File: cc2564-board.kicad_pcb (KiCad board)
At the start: 2 copper layers, 45 parts, among them J1 TYPE-C-31-M-12, J2 Conn_ARM_JTAG_SWD_10, J4 BOOT1, J5 BOOT0, J6 Conn_01x16, J7 Conn_01x16, U1 LD1117#33, U2 LD1117#18, U3 STM32F103C8Tx, U4 CC2564CRVMR, U5 TXB0104D

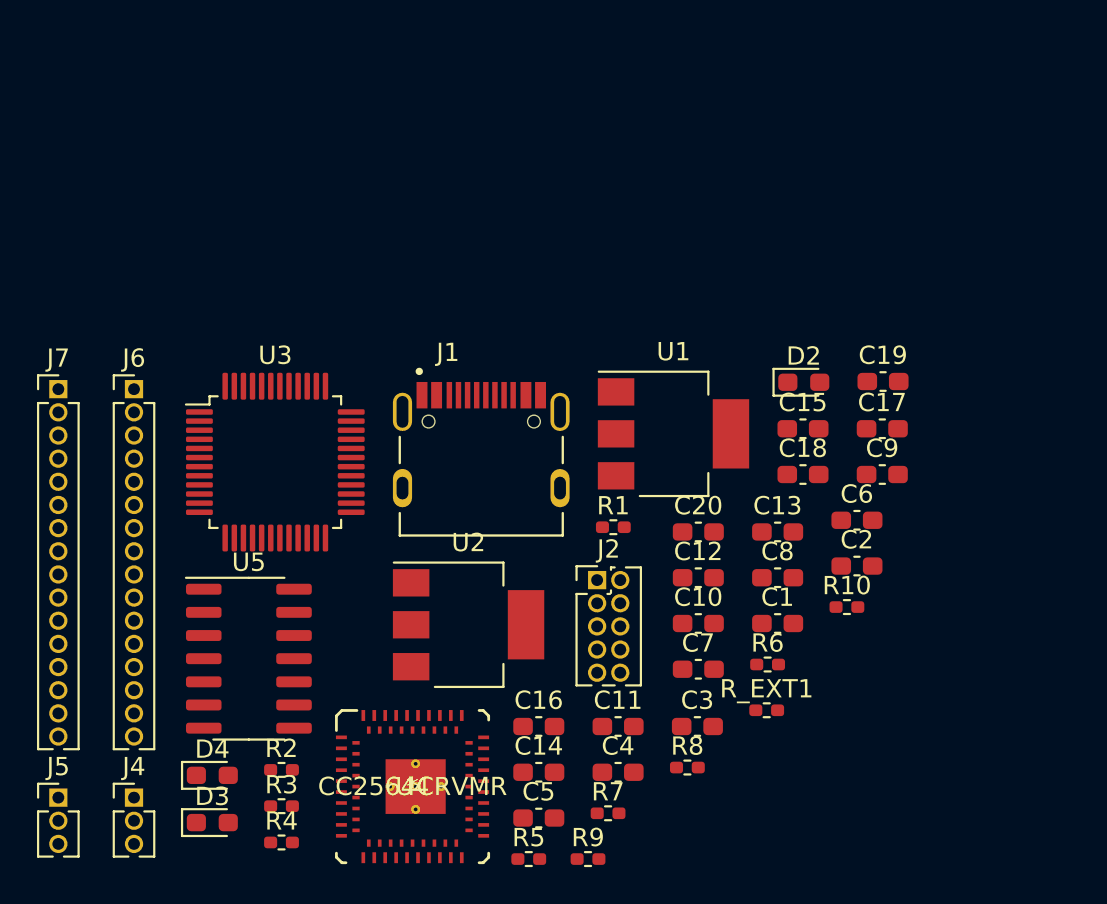
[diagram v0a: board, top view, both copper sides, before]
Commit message: RF matching placeholder and filtering
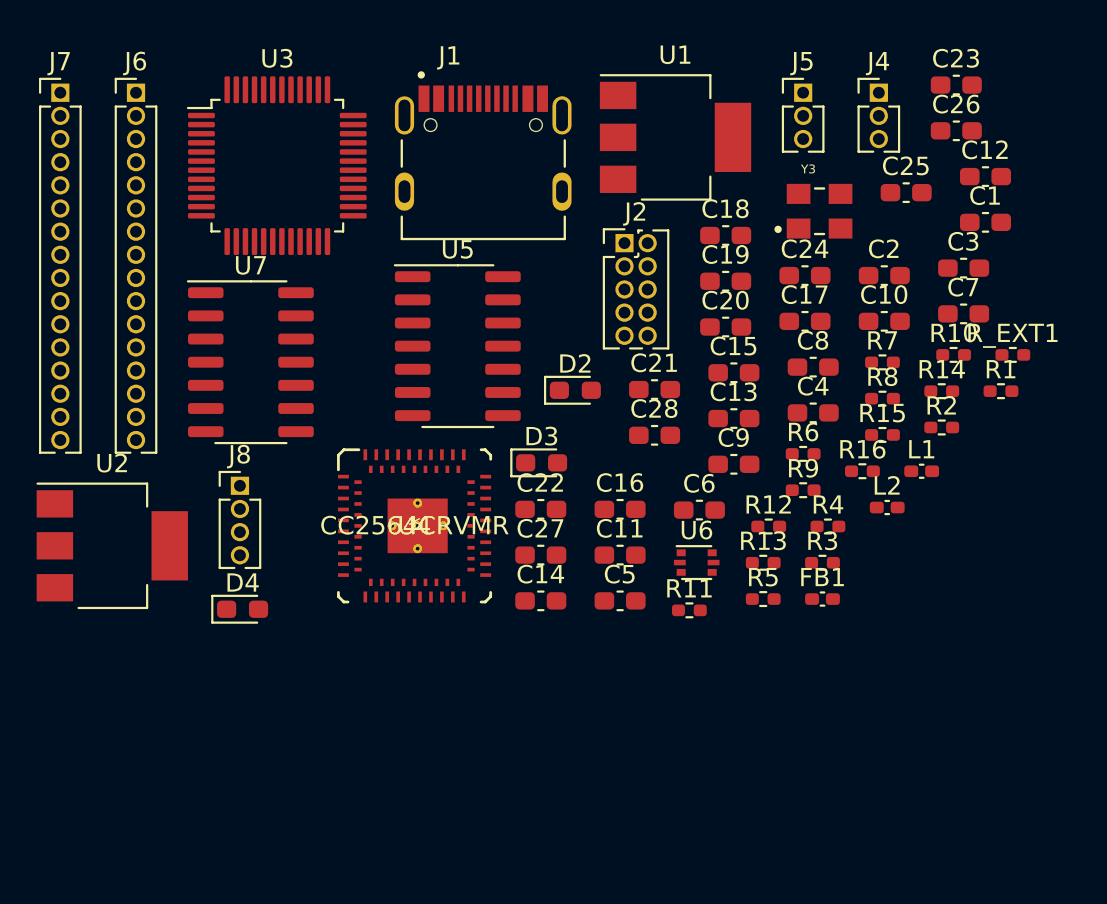
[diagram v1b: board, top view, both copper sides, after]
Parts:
- added C21: 10 pF, Capacitor_SMD:C_0603_1608Metric_Pad1.08x0.95mm_HandSolder, F.Cu at (131.4, 80.0)
- added C22: 10 pF, Capacitor_SMD:C_0603_1608Metric_Pad1.08x0.95mm_HandSolder, F.Cu at (125.2, 86.5)
- added C23: 0.1uF, Capacitor_SMD:C_0603_1608Metric_Pad1.08x0.95mm_HandSolder, F.Cu at (148.0, 63.3)
- added C24: 0.1uF, Capacitor_SMD:C_0603_1608Metric_Pad1.08x0.95mm_HandSolder, F.Cu at (139.7, 73.7)
- added C25: 0.1uF, Capacitor_SMD:C_0603_1608Metric_Pad1.08x0.95mm_HandSolder, F.Cu at (145.2, 69.2)
- added C26: DNP, Capacitor_SMD:C_0603_1608Metric_Pad1.08x0.95mm_HandSolder, F.Cu at (148.0, 65.8)
- added C27: DNP, Capacitor_SMD:C_0603_1608Metric_Pad1.08x0.95mm_HandSolder, F.Cu at (125.2, 89.0)
- added C28: 22pF, Capacitor_SMD:C_0603_1608Metric_Pad1.08x0.95mm_HandSolder, F.Cu at (131.4, 82.5)
- added FB1: BK1005HS680-T‎, Inductor_SMD:L_0402_1005Metric_Pad0.77x0.64mm_HandSolder, F.Cu at (140.7, 91.5)
- added J8: Conn_01x04, Connector_PinHeader_1.27mm:PinHeader_1x04_P1.27mm_Vertical, F.Cu at (108.7, 85.2)
- added L1: 27nH, Inductor_SMD:L_0402_1005Metric_Pad0.77x0.64mm_HandSolder, F.Cu at (146.1, 84.5)
- added L2: 0ohm, Inductor_SMD:L_0402_1005Metric_Pad0.77x0.64mm_HandSolder, F.Cu at (144.2, 86.4)
- added R11: 10k, Resistor_SMD:R_0402_1005Metric_Pad0.72x0.64mm_HandSolder, F.Cu at (133.4, 92.1)
- added R12: 10k, Resistor_SMD:R_0402_1005Metric_Pad0.72x0.64mm_HandSolder, F.Cu at (137.7, 87.5)
- added R13: 0, Resistor_SMD:R_0402_1005Metric_Pad0.72x0.64mm_HandSolder, F.Cu at (137.4, 89.5)
- added R14: 0, Resistor_SMD:R_0402_1005Metric_Pad0.72x0.64mm_HandSolder, F.Cu at (147.2, 80.1)
- added R15: 0, Resistor_SMD:R_0402_1005Metric_Pad0.72x0.64mm_HandSolder, F.Cu at (143.9, 82.5)
- added R16: 0, Resistor_SMD:R_0402_1005Metric_Pad0.72x0.64mm_HandSolder, F.Cu at (142.8, 84.5)
- added U6: USBLC6-2P6, Package_TO_SOT_SMD:SOT-666, F.Cu at (133.8, 89.5)
- added U7: TXB0104D, Package_SO:SOIC-14_3.9x8.7mm_P1.27mm, F.Cu at (109.3, 78.5)
- added Y3: ECS-327MVATX-3-CN-TR, cc2654-board-footprints:OSC_ECS-2333-160-BN-TR, F.Cu at (140.5, 70.2)
- D4: value LED -> GREEN 150060GS75000
- R1: value 1.5k -> 10k
- R10: value R -> 90
- R3: value 22 -> 1.5k
- R4: value 22 -> 0
- R8: value R -> 55
- R9: value R -> 4
- moved J4 56.2 mm to (143.8, 63.7)
- moved J5 56.2 mm to (139.6, 63.7)
- moved R2 40.8 mm to (147.2, 82.0)
- moved R4 34.6 mm to (141.0, 87.5)
- moved R3 32.5 mm to (140.7, 89.5)
- moved C3 29.1 mm to (148.4, 73.3)
- moved R7 28.9 mm to (143.9, 78.5)
- moved C12 27.1 mm to (149.6, 68.3)
- moved D3 26.7 mm to (125.3, 84.0)
- moved C1 24.8 mm to (149.6, 70.8)
- moved C7 24.3 mm to (148.4, 75.8)
- moved R_EXT1 23.7 mm to (151.1, 78.1)
- moved R9 23.4 mm to (139.6, 85.5)
- moved R8 22.9 mm to (143.9, 80.5)
- moved R1 22.5 mm to (150.4, 80.1)
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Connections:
- net Net-(U4-PadA35) renamed BT_AUD_FSYNC
- net Net-(U4-PadB32) renamed BT_AUD_CLK
- net Net-(U4-PadB33) renamed BT_AUD_OUT
- net Net-(U4-PadB34) renamed BT_AUD_IN
- C1 pad 2: Net-(C1-Pad2) -> VCC_USB
- C11 pad 1: VDD_3V3 -> VDDA_3V3
- C12 pad 1: VDD_3V3 -> VDDA_3V3
- C17 pad 1: Net-(C17-Pad1) -> GND
- C17 pad 2: GND -> Net-(C17-Pad2)
- C8 pad 2: Net-(C1-Pad2) -> VCC_USB
- J1 pad A6: USBDP -> USB_CONN_D+
- J1 pad A7: USBDM -> USB_CONN_D-
- J1 pad B6: Net-(J1-PadB6) -> USB_CONN_D+
- J1 pad B7: Net-(J1-PadB7) -> USB_CONN_D-
- J7 pad 12: USBDM -> USB_D-
- J7 pad 13: USBDP -> USB_D+
- R1 pad 2: USBDP -> Net-(R1-Pad2)
- R3 pad 1: Net-(J1-PadB7) -> VDD_3V3
- R3 pad 2: USBDM -> USB_D+
- R4 pad 1: USBDP -> Net-(R4-Pad1)
- R4 pad 2: Net-(J1-PadB6) -> USB_D-
- R_EXT1 pad 2: GND -> Net-(C18-Pad2)
- U1 pad 3: Net-(C1-Pad2) -> VCC_USB
- U2 pad 3: Net-(C1-Pad2) -> VCC_USB
- U3 pad 32: USBDM -> Net-(R4-Pad1)
- U3 pad 33: USBDP -> Net-(R14-Pad2)
- U3 pad 5: Net-(C17-Pad1) -> Net-(C17-Pad2)
- U3 pad 9: VDD_3V3 -> VDDA_3V3
- U4 pad A25: Net-(U4-PadA25) -> BT_SLOW_CLK
- U4 pad A3: Net-(U4-PadA3) -> Net-(U4-PadA2)
- U4 pad A6: Net-(U4-PadA6) -> NSHUTDOWN_1V8
- U4 pad A9: Net-(U4-PadA9) -> Net-(U4-PadA5)
- U4 pad B15: Net-(U4-PadB15) -> Net-(U4-PadA2)
- U4 pad B2: Net-(U4-PadB2) -> Net-(U4-PadA5)
- U4 pad B24: TX_DBG -> BT_TX_DBG
- U4 pad B26: Net-(U4-PadB26) -> Net-(U4-PadA2)
- U4 pad B27: Net-(U4-PadB27) -> Net-(U4-PadA2)
- U4 pad B35: Net-(U4-PadB35) -> Net-(U4-PadA2)
- U4 pad B36: Net-(U4-PadB36) -> Net-(U4-PadA2)
- U4 pad B4: Net-(U4-PadB4) -> GND
- U4 pad B6: Net-(U4-PadB6) -> Net-(U4-PadB5)
- U4 pad B7: Net-(U4-PadB7) -> Net-(U4-PadA5)

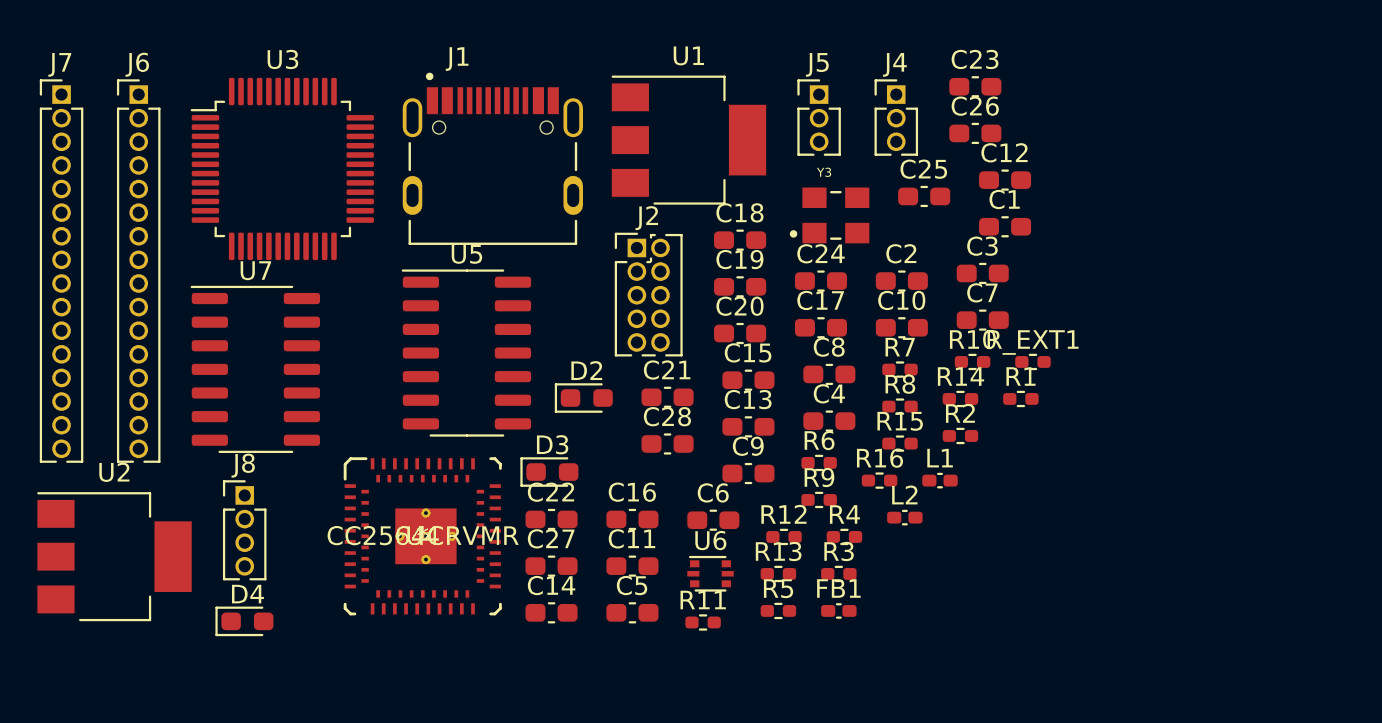
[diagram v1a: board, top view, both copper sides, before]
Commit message: Fix up a bunch of footprints
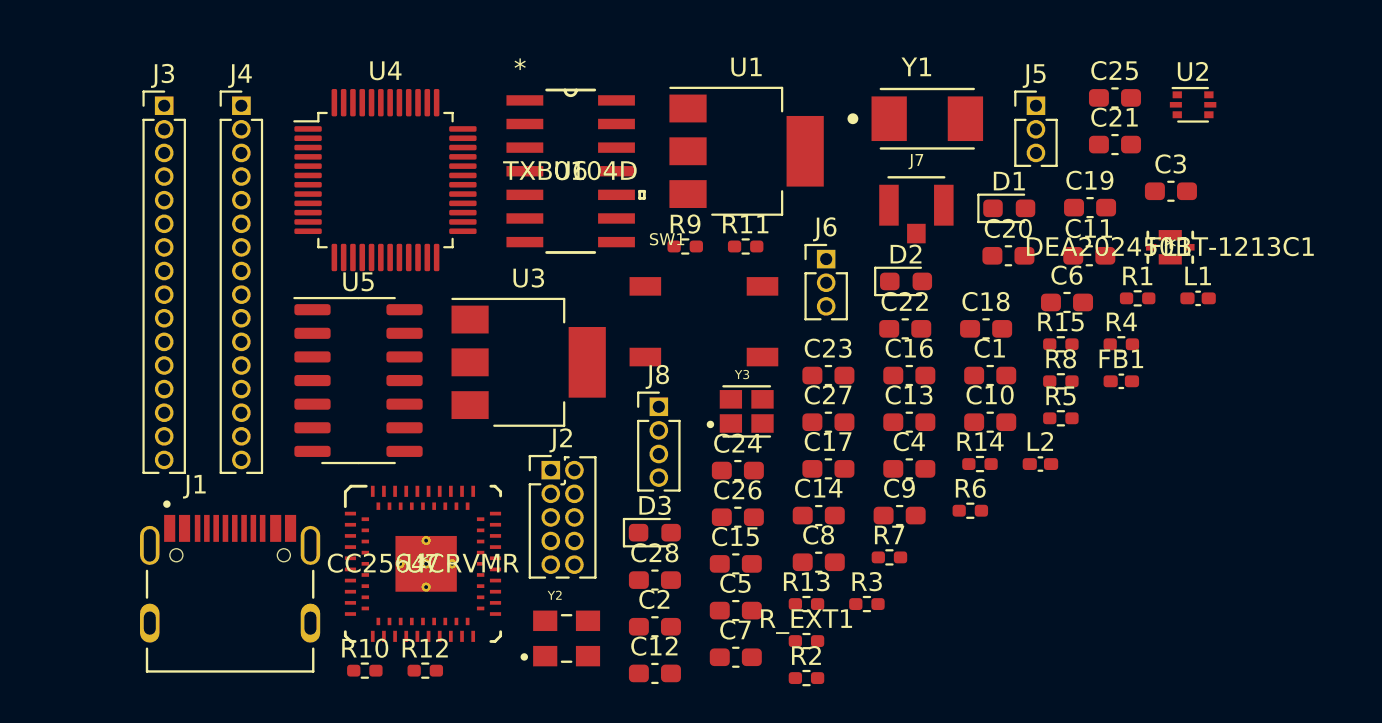
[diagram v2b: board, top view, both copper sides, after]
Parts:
- removed D4: GREEN 150060GS75000, LED_SMD:LED_0603_1608Metric_Pad1.05x0.95mm_HandSolder
- removed R16: 0, Resistor_SMD:R_0402_1005Metric_Pad0.72x0.64mm_HandSolder
- added D1: GREEN 150060GS75000, LED_SMD:LED_0603_1608Metric_Pad1.05x0.95mm_HandSolder, F.Cu at (149.8, 69.8)
- added FL1: DEA202450BT-1213C1, cc2654-board-footprints:DEA202450BT-1213C1, F.Cu at (158.5, 71.9)
- added J3: Conn_01x16, Connector_PinHeader_1.27mm:PinHeader_1x16_P1.27mm_Vertical, F.Cu at (104.4, 64.3)
- added SW1: SW_Push, cc2654-board-footprints:TL3342F160QG_TR, F.Cu at (133.4, 75.9)
- added Y1: ECS-80-18-30-JGN-TR, cc2654-board-footprints:XTAL_ECS-80-18-30-JGN-TR, F.Cu at (145.4, 65.0)
- added Y2: ECS-327MVATX-3-CN-TR, cc2654-board-footprints:OSC_ECS-2333-160-BN-TR, F.Cu at (126.0, 92.9)
- C10: value 100nF -> 0.1uF
- C12: value 1uF -> 10uF
- C13: value 0.1uF -> 100nF
- C17: value 20 pF -> 0.1uF
- C19: value 0.1uF -> 20 pF
- C20: value 0.1uF -> DNP
- C21: value 10 pF -> DNP
- C22: value 10 pF -> 22pF
- C26: value DNP -> 0.1uF
- C27: value DNP -> 10 pF
- C28: value 22pF -> 10 pF
- C9: value 10uF -> 1uF
- J4: value BOOT1 -> Conn_01x16; footprint Connector_PinHeader_1.27mm:PinHeader_1x03_P1.27mm_Vertical -> Connector_PinHeader_1.27mm:PinHeader_1x16_P1.27mm_Vertical
- J5: value BOOT0 -> BOOT1
- J6: value Conn_01x16 -> BOOT0; footprint Connector_PinHeader_1.27mm:PinHeader_1x16_P1.27mm_Vertical -> Connector_PinHeader_1.27mm:PinHeader_1x03_P1.27mm_Vertical
- J7: value Conn_01x16 -> 1909763-1; footprint Connector_PinHeader_1.27mm:PinHeader_1x16_P1.27mm_Vertical -> cc2654-board-footprints:UFL-TE_1909763-1
- R1: value 10k -> 5.1k
- R10: value 90 -> 0
- R11, R12: value 10k -> 0
- R14, R7: value 0 -> 10k
- R2: value 5.1k -> 0
- R3: value 1.5k -> 5.1k
- R4: value 0 -> 90
- R5: value 0 -> 55
- R6: value 5.1k -> 4
- R8: value 55 -> 10k
- R9: value 4 -> 1.5k
- U2: value LD1117#18 -> USBLC6-2P6; footprint Package_TO_SOT_SMD:SOT-223-3_TabPin2 -> Package_TO_SOT_SMD:SOT-666
- U3: value STM32F103C8Tx -> LD1117#18; footprint Package_QFP:LQFP-48_7x7mm_P0.5mm -> Package_TO_SOT_SMD:SOT-223-3_TabPin2
- U4: value CC2564CRVMR -> STM32F103C8Tx; footprint cc2654-board-footprints:CC2564CRVMR -> Package_QFP:LQFP-48_7x7mm_P0.5mm
- U6: value USBLC6-2P6 -> TXB0104D; footprint Package_TO_SOT_SMD:SOT-666 -> cc2654-board-footprints:TXB0104D
- U7: value TXB0104D -> CC2564CRVMR; footprint Package_SO:SOIC-14_3.9x8.7mm_P1.27mm -> cc2654-board-footprints:CC2564CRVMR
- Y3: value ECS-327MVATX-3-CN-TR -> ECS-260-8-36CKM-TR; footprint cc2654-board-footprints:OSC_ECS-2333-160-BN-TR -> cc2654-board-footprints:XTAL_ECS-160-10-36-JGN-TR
- moved U2 62.9 mm to (159.7, 64.2)
- moved J7 46.4 mm to (144.8, 69.6)
- moved J6 38.0 mm to (140.0, 72.5)
- moved R10 36.7 mm to (115.2, 94.7)
- moved J4 35.2 mm to (108.5, 64.3)
- moved C12 32.5 mm to (130.8, 94.8)
- moved C11 29.7 mm to (154.1, 72.4)
- moved C21 27.6 mm to (155.5, 66.4)
- moved J1 27.0 mm to (107.9, 92.1)
- moved C26 24.3 mm to (135.2, 86.4)
- moved U6 22.9 mm to (126.2, 67.8)
- moved C2 22.8 mm to (130.8, 92.3)
- moved J8 22.8 mm to (131.0, 80.5)
- moved C7 22.5 mm to (135.1, 94.0)
- moved C6 22.3 mm to (152.9, 74.9)
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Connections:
- C10 pad 1: Net-(C10-Pad1) -> VDD_1V8_32K
- C11 pad 1: VDDA_3V3 -> GND
- C11 pad 2: GND -> VCC_USB
- C12 pad 1: VDDA_3V3 -> GND
- C12 pad 2: GND -> VDD_1V8
- C13 pad 1: VDD_1V8 -> SWD_NRST
- C14 pad 1: VDD_1V8 -> GND
- C14 pad 2: GND -> VDD_3V3
- C15 pad 1: VDD_1V8 -> GND
- C15 pad 2: GND -> VDD_1V8
- C16 pad 1: VDD_1V8 -> GND
- C16 pad 2: GND -> VDD_3V3
- C17 pad 2: Net-(C17-Pad2) -> VDD_1V8
- C19 pad 2: VDD_3V3 -> Net-(C19-Pad2)
- C20 pad 1: GND -> Net-(C20-Pad1)
- C20 pad 2: VDD_1V8 -> GND
- C21 pad 1: GND -> Net-(C21-Pad1)
- C22 pad 1: GND -> Net-(C22-Pad1)
- C23 pad 1: VDD_1V8_32K -> VDD_1V8
- C24 pad 1: GND -> VDD_1V8
- C24 pad 2: VDD_3V3 -> GND
- C25 pad 1: GND -> VDD_1V8
- C25 pad 2: VDD_1V8 -> GND
- C26 pad 1: GND -> VDD_1V8
- C27 pad 1: Net-(C27-Pad1) -> GND
- C28 pad 1: Net-(C28-Pad1) -> GND
- C8 pad 1: GND -> VDDA_3V3
- C8 pad 2: VCC_USB -> GND
- C9 pad 1: GND -> VDDA_3V3
- C9 pad 2: VDD_1V8 -> GND
- J4 pad 1: VDD_3V3 -> USART2_CTS
- J4 pad 2: BOOT1 -> USART2_RTS
- J4 pad 3: GND -> USART2_TX
- J5 pad 2: BOOT0 -> BOOT1
- J6 pad 1: PB0 -> VDD_3V3
- J6 pad 2: PB1 -> BOOT0
- J6 pad 3: BOOT1 -> GND
- J7 pad 1: USART2_CTS -> Net-(J7-Pad1)
- J7 pad 2: USART2_RTS -> GND
- J7 pad 3: USART2_TX -> GND
- L2 pad 1: GND -> Net-(C20-Pad1)
- L2 pad 2: Net-(C27-Pad1) -> Net-(C21-Pad1)
- R1 pad 1: VDD_3V3 -> Net-(J1-PadA5)
- R1 pad 2: Net-(R1-Pad2) -> GND
- R10 pad 1: VCC_USB -> Net-(R10-Pad1)
- R10 pad 2: Net-(D4-Pad2) -> USB_D-
- R11 pad 1: VDD_3V3 -> USB_D+
- R12 pad 1: VDD_1V8_32K -> Net-(AE1-Pad1)
- R12 pad 2: Net-(R12-Pad2) -> Net-(C21-Pad1)
- R13 pad 1: BT_SLOW_CLK -> Net-(J7-Pad1)
- R13 pad 2: Net-(R13-Pad2) -> Net-(C21-Pad1)
- R14 pad 1: USB_D+ -> VDD_1V8_32K
- R15 pad 1: Net-(AE1-Pad1) -> BT_SLOW_CLK
- R15 pad 2: Net-(C27-Pad1) -> Net-(R15-Pad2)
- R2 pad 1: Net-(J1-PadA5) -> SWD_NRST
- R2 pad 2: GND -> Net-(J2-Pad10)
- R3 pad 1: VDD_3V3 -> Net-(J1-PadB5)
- R3 pad 2: USB_D+ -> GND
- R4 pad 1: Net-(R4-Pad1) -> VCC_USB
- R4 pad 2: USB_D- -> Net-(D1-Pad2)
- R5 pad 1: SWD_NRST -> VDD_3V3
- R5 pad 2: Net-(J2-Pad10) -> Net-(D2-Pad2)
- R6 pad 1: Net-(J1-PadB5) -> VDD_1V8
- R6 pad 2: GND -> Net-(D3-Pad2)
- R7 pad 1: Net-(C10-Pad1) -> VDD_3V3
- R7 pad 2: SWD_NRST -> Net-(R7-Pad2)
- R8 pad 2: Net-(D2-Pad2) -> Net-(R8-Pad2)
- R9 pad 1: VDD_1V8 -> VDD_3V3
- R9 pad 2: Net-(D3-Pad2) -> USB_D+
- R_EXT1 pad 2: Net-(C18-Pad2) -> Net-(C19-Pad2)
- U2 pad 1: GND -> USB_D-
- U2 pad 2: VDD_1V8 -> GND
- U2 pad 3: VCC_USB -> USB_D+
- U3 pad 1: VDD_3V3 -> GND
- U3 pad 2: Net-(U3-Pad2) -> VDD_1V8
- U3 pad 3: Net-(U3-Pad3) -> VCC_USB
- U5 pad 10: USART2_RX_1V8 -> Net-(U5-Pad10)
- U5 pad 11: USART2_TX_1V8 -> Net-(U5-Pad11)
- U5 pad 12: USART2_RTS_1V8 -> Net-(U5-Pad12)
- U5 pad 13: USART2_CTS_1V8 -> NSHUTDOWN_1V8
- U5 pad 2: USART2_CTS -> NSHUTDOWN
- U5 pad 3: USART2_RTS -> Net-(U5-Pad3)
- U5 pad 4: USART2_TX -> Net-(U5-Pad4)
- U5 pad 5: USART2_RX -> Net-(U5-Pad5)
- U5 pad 8: Net-(R11-Pad2) -> Net-(R7-Pad2)
- U6 pad 1: USB_D- -> VDD_3V3
- U6 pad 2: GND -> USART2_CTS
- U6 pad 3: USB_D+ -> USART2_RTS
- U6 pad 4: USB_CONN_D+ -> USART2_TX
- U6 pad 5: VCC_USB -> USART2_RX
- U6 pad 6: USB_CONN_D- -> Net-(U6-Pad6)
- Y3 pad 1: Net-(R12-Pad2) -> GND
- Y3 pad 3: Net-(R13-Pad2) -> Net-(C28-Pad2)
- Y3 pad 4: VDD_1V8_32K -> GND
